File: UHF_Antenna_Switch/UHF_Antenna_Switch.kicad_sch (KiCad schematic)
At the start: 27 parts, among them J1 Conn_N_Type_Female, J2 Conn_SO-239, J3 Conn_SMA_Female, J4 Screw_Terminal_01x02, SW1 SW_SP3T, U1 LTC5507ES6, U2 PAT1220-C-10DB, U3 X4C09F1-30S, U4 RP2040-Zero

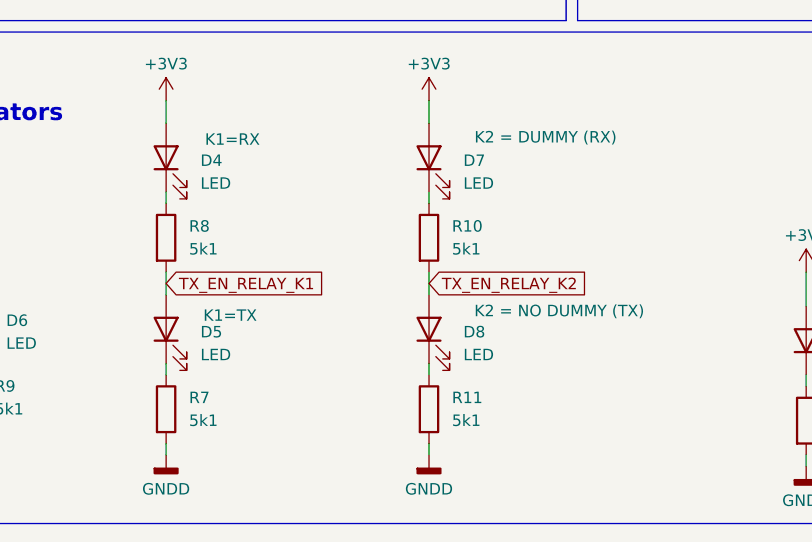
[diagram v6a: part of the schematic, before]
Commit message: Add preliminary footprint to directional coupler and begin layout
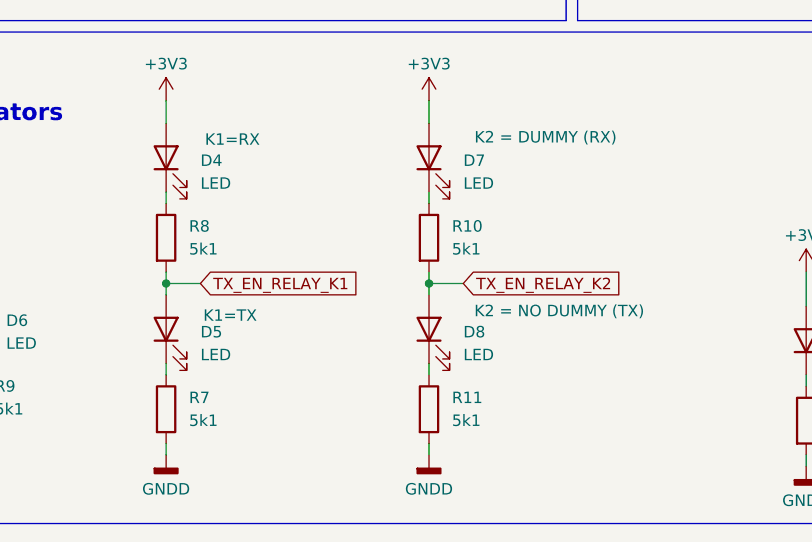
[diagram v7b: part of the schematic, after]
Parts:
- U3: footprint (none) -> 00-project-footprints:X4C09F1 - 30S
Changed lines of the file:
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@@
+	)
+	(junction
+		(at 87.63 171.45)
+		(diameter 0)
+		(color 0 0 0 0)
+	)
+	(junction
+		(at 58.42 171.45)
+		(diameter 0)
+		(color 0 0 0 0)
 	)
 	(junction
@@
 		)
 	)
+	(wire
+		(pts
+			(xy 91.44 171.45) (xy 87.63 171.45)
+		)
+		(stroke
+			(width 0)
+			(type default)
+		)
+	)
 	(polyline
 		(pts
@@
 	(wire
 		(pts
+			(xy 62.23 171.45) (xy 58.42 171.45)
+		)
+		(stroke
+			(width 0)
+			(type default)
+		)
+	)
+	(wire
+		(pts
 			(xy 64.77 110.49) (xy 74.93 110.49)
 		)
@@
 	(wire
 		(pts
-			(xy 58.42 170.18) (xy 58.42 172.72)
+			(xy 58.42 170.18) (xy 58.42 171.45)
 		)
 		(stroke
@@
 	(wire
 		(pts
-			(xy 87.63 170.18) (xy 87.63 172.72)
+			(xy 87.63 170.18) (xy 87.63 171.45)
 		)
 		(stroke
@@
 		(pts
 			(xy 64.77 107.95) (xy 74.93 107.95)
+		)
+		(stroke
+			(width 0)
+			(type default)
+		)
+	)
+	(wire
+		(pts
+			(xy 87.63 171.45) (xy 87.63 172.72)
 		)
 		(stroke
@@
 		(pts
 			(xy 114.3 57.15) (xy 119.38 57.15)
+		)
+		(stroke
+			(width 0)
+			(type default)
+		)
+	)
+	(wire
+		(pts
+			(xy 58.42 171.45) (xy 58.42 172.72)
 		)
 		(stroke
@@
 	(global_label "TX_EN_RELAY_K1"
 		(shape input)
-		(at 58.42 171.45 0)
+		(at 62.23 171.45 0)
 		(fields_autoplaced yes)
 		(effects
@@
 		)
 		(property "Intersheetrefs" "${INTERSHEET_REFS}"
-			(at 77.0684 171.45 0)
+			(at 80.8784 171.45 0)
 			(hide yes)
 			(show_name no)
@@
 	(global_label "TX_EN_RELAY_K2"
 		(shape input)
-		(at 87.63 171.45 0)
+		(at 91.44 171.45 0)
 		(fields_autoplaced yes)
 		(effects
@@
 		)
 		(property "Intersheetrefs" "${INTERSHEET_REFS}"
-			(at 106.2784 171.45 0)
+			(at 110.0884 171.45 0)
 			(hide yes)
 			(show_name no)
@@
 			)
 		)
-		(property "Footprint" ""
+		(property "Footprint" "00-project-footprints:X4C09F1 - 30S"
 			(at 80.01 58.42 0)
 			(hide yes)

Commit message: Rename X4C09F1-30S footprint with no space
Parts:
- U3: footprint 00-project-footprints:X4C09F1 - 30S -> 00-project-footprints:X4C09F1-30S
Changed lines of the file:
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@@
 			)
 		)
-		(property "Footprint" "00-project-footprints:X4C09F1 - 30S"
+		(property "Footprint" "00-project-footprints:X4C09F1-30S"
 			(at 80.01 58.42 0)
 			(hide yes)
